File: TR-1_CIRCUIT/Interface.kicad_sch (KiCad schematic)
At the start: 4 parts

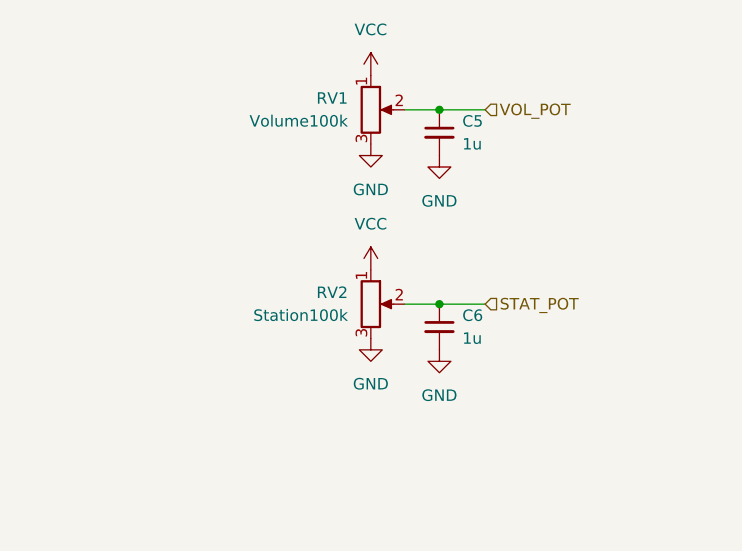
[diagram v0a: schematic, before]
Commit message: finished the overall design and swapped out the pot for an encoder
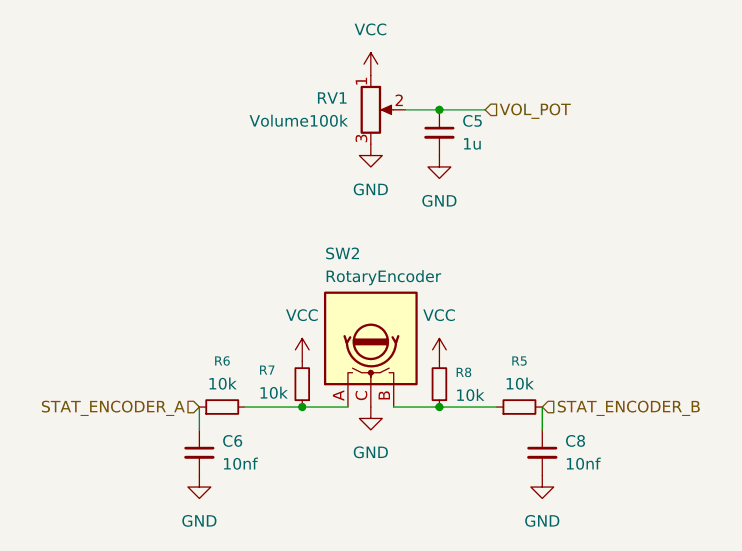
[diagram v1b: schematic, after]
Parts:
- removed RV2: Station100k, symbol Device:R_Potentiometer
- added C8: 10nf, symbol Device:C_Small
- added R5, R6, R7, R8: 10k, symbol Device:R_Small
- added SW2: RotaryEncoder, symbol Device:RotaryEncoder
- C6: value 1u -> 10nf
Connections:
- net GND: now also C8.2, SW2.C
- net VCC: now also R7.2, R8.2
- net STAT_POT renamed STAT_ENCODER_A
- net STAT_ENCODER_A: now also R6.1
- new net: R5.1, R8.1, SW2.B
- new net: R6.2, R7.1, SW2.A
- new net STAT_ENCODER_B: C8.1, R5.2
